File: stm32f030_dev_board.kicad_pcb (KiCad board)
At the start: 4 copper layers, 85 x 55 mm, 66 parts, among them J2 Conn_01x16, J3 Conn_01x16, J4 Conn_01x16, J5 Conn_01x06, J6 Conn_01x04, J7 USB_C_Receptacle_USB2.0_16P, Q1 DMP3099L, Q2 DMP3099L, SW1 SW_Push, SW3 SW_Push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

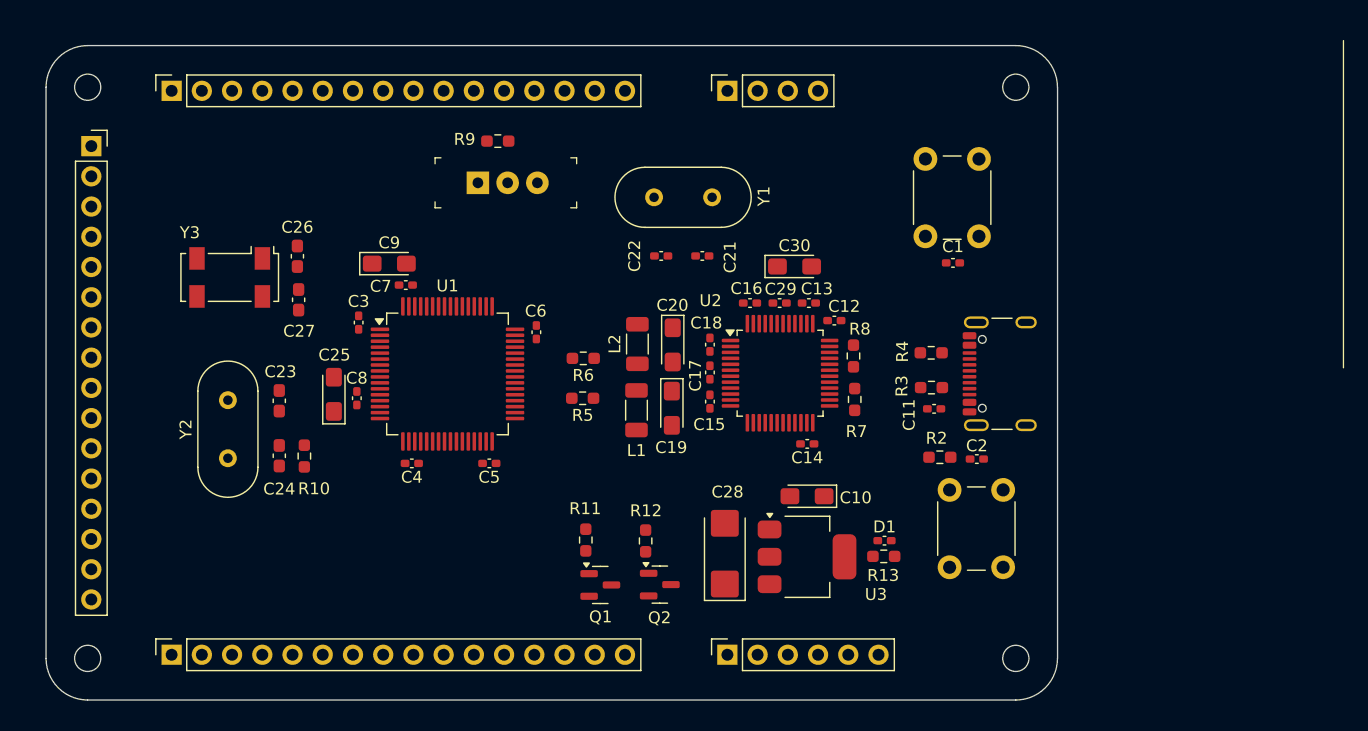
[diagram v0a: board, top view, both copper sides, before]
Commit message: Adjusted Spacing between pin headers
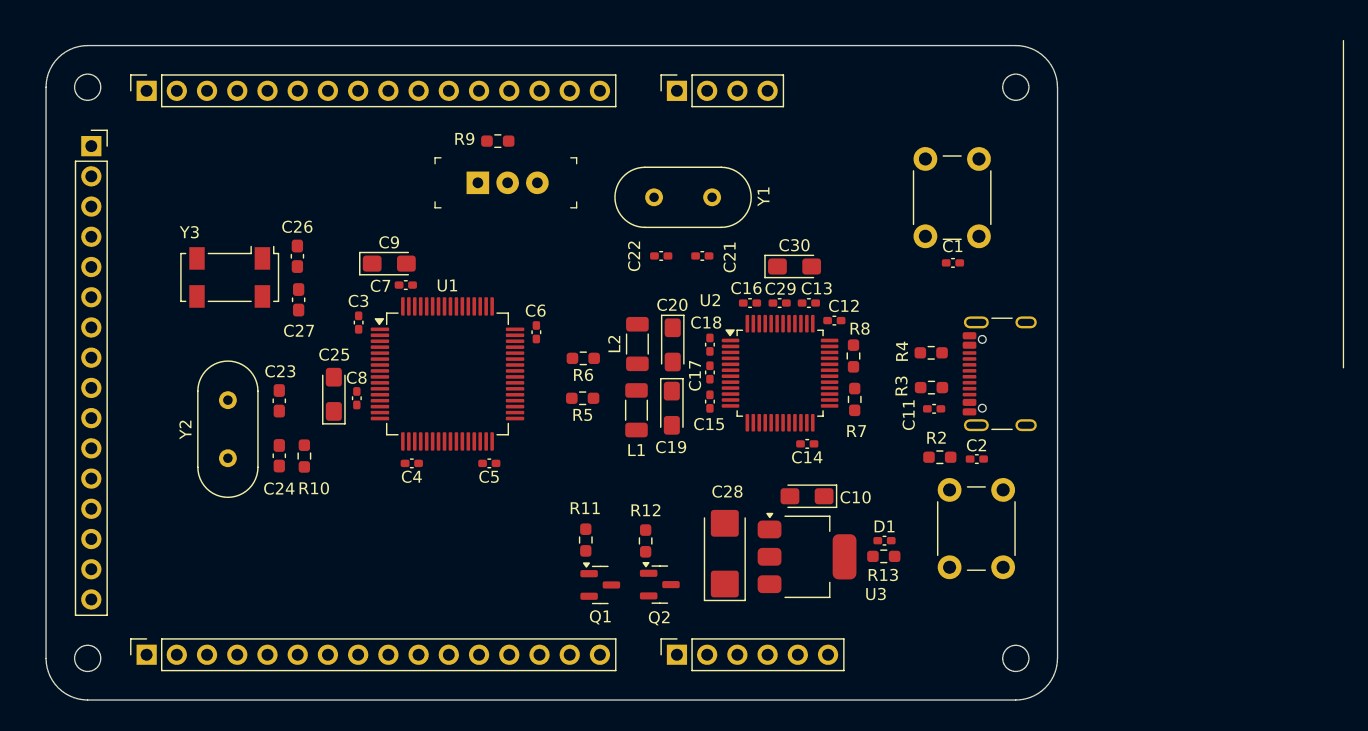
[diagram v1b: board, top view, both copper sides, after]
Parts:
- moved J5 4.24 mm to (143.0, 121.2)
- moved J6 4.24 mm to (143.0, 73.8)
- moved J2 2.11 mm to (98.5, 121.2)
- moved J3 2.11 mm to (98.5, 73.8)
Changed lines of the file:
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@@
 	(footprint "Connector_PinSocket_2.54mm:PinSocket_1x04_P2.54mm_Vertical"
 		(layer "F.Cu")
-		(at 147.26 73.803 90)
+		(at 143.02 73.803 90)
 		(descr "Through hole straight socket strip, 1x04, 2.54mm pitch, single row (from Kicad 4.0.7), script generated")
 		(tags "Through hole socket strip THT 1x04 2.54mm single row")
@@
 			(at 0 10.39 90)
 			(layer "F.Fab")
+			(hide yes)
 			(effects
 				(font
@@
 	(footprint "Connector_PinSocket_2.54mm:PinSocket_1x06_P2.54mm_Vertical"
 		(layer "F.Cu")
-		(at 147.26 121.197 90)
+		(at 143.02 121.197 90)
 		(descr "Through hole straight socket strip, 1x06, 2.54mm pitch, single row (from Kicad 4.0.7), script generated")
 		(tags "Through hole socket strip THT 1x06 2.54mm single row")
@@
 			(at 0 3.2 0)
 			(layer "F.Fab")
+			(hide yes)
 			(effects
 				(font
@@
 			(unlocked yes)
 			(layer "F.Fab")
+			(hide yes)
 			(effects
 				(font
@@
 	(footprint "Connector_PinSocket_2.54mm:PinSocket_1x16_P2.54mm_Vertical"
 		(layer "F.Cu")
-		(at 100.555 73.803 90)
+		(at 98.45 73.803 90)
 		(descr "Through hole straight socket strip, 1x16, 2.54mm pitch, single row (from Kicad 4.0.7), script generated")
 		(tags "Through hole socket strip THT 1x16 2.54mm single row")
@@
 			(at 0 40.87 90)
 			(layer "F.Fab")
+			(hide yes)
 			(effects
 				(font
@@
 	(footprint "Connector_PinSocket_2.54mm:PinSocket_1x16_P2.54mm_Vertical"
 		(layer "F.Cu")
-		(at 100.555 121.197 90)
+		(at 98.45 121.197 90)
 		(descr "Through hole straight socket strip, 1x16, 2.54mm pitch, single row (from Kicad 4.0.7), script generated")
 		(tags "Through hole socket strip THT 1x16 2.54mm single row")
@@
 			(at 0 3.2 0)
 			(layer "F.Fab")
+			(hide yes)
 			(effects
 				(font

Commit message: removed D+ and D- resistors, finished routing front and back copper, moved button to better place
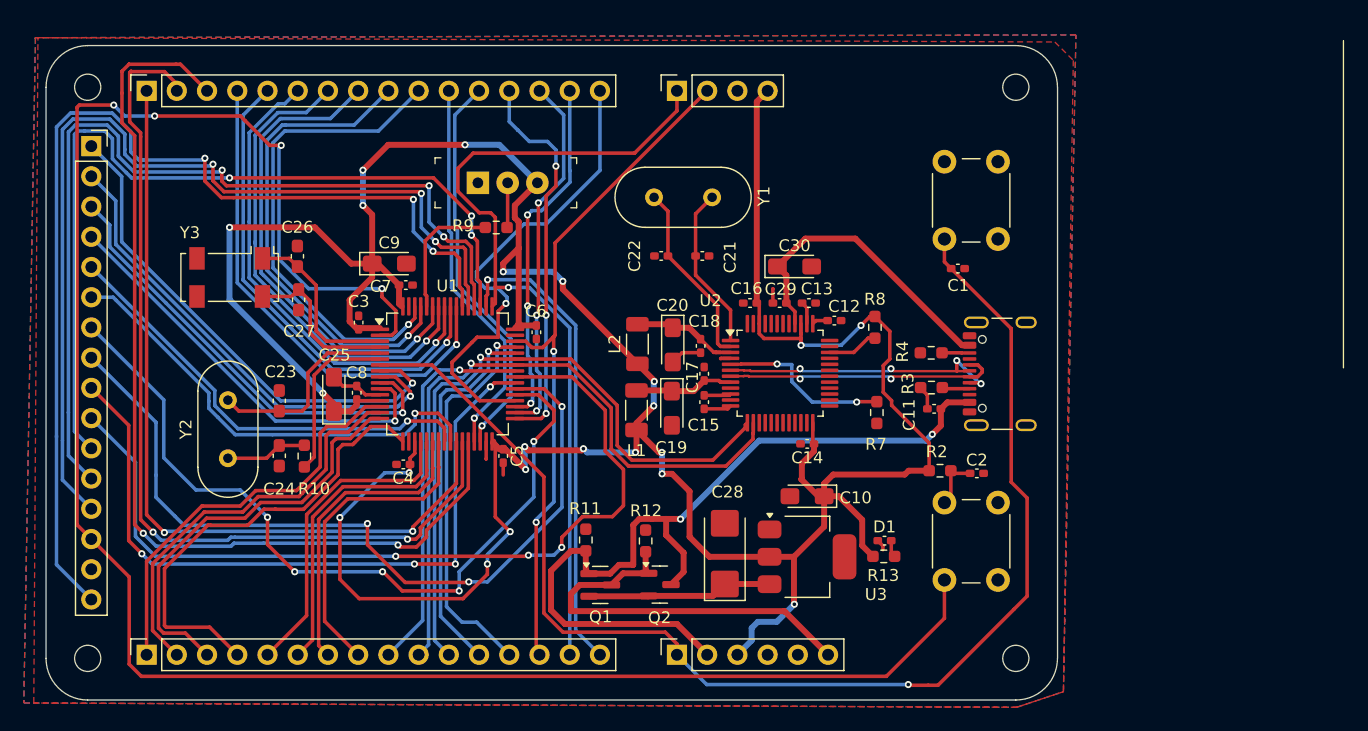
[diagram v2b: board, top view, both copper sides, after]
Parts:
- removed R5, R6: 22, Resistor_SMD:R_0603_1608Metric_Pad0.98x0.95mm_HandSolder
- moved R9 7.26 mm to (127.8, 85.3)
- moved R8 3.01 mm to (159.7, 93.7)
- moved R7 2.16 mm to (159.8, 100.8), turned to -90 degrees
- moved SW1 1.61 mm to (170.0, 79.8)
- moved C5 1.32 mm to (128.4, 104.5), turned to -90 degrees
- moved C2 1.20 mm to (168.2, 106.0)
- moved SW3 1.15 mm to (170.0, 108.4)
- moved R2 1.13 mm to (165.1, 105.7)
- moved C18 0.79 mm to (145.0, 95.2)
- moved C4 0.72 mm to (120.0, 105.2)
- moved C1 0.63 mm to (166.6, 88.7)
- moved C17 0.50 mm to (145.3, 97.6)
- moved C15 0.48 mm to (145.3, 100.0)
- moved C8 0.46 mm to (116.1, 99.2)
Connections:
- J4 pad 15: unconnected-(J4-Pin_15-Pad15) -> GND
- U2 pad 6: /DM -> /D-
- U2 pad 7: /DP -> /D+
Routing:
- net +3.3V: track 0.00 -> 288.2 mm, vias 0 -> 22
- net /PC13: track 0.00 -> 170.9 mm, vias 0 -> 4
- net /NRST: track 0.00 -> 108.8 mm, vias 0 -> 1
- net +5V: track 0.00 -> 97.2 mm, vias 0 -> 2
- net /PD2: track 0.00 -> 88.3 mm, vias 0 -> 3
- net /PB2: track 0.00 -> 82.2 mm, vias 0 -> 2
- net /PC12: track 0.00 -> 80.1 mm, vias 0 -> 3
- net /PC11: track 0.00 -> 76.9 mm, vias 0 -> 3
- net /PB1: track 0.00 -> 76.9 mm, vias 0 -> 2
- net /PC9: track 0.00 -> 72.8 mm, vias 0 -> 3
- net /PC10: track 0.00 -> 72.3 mm, vias 0 -> 3
- net /SWCLK: track 0.00 -> 70.8 mm, vias 0 -> 1
- net /PC7: track 0.00 -> 67.9 mm, vias 0 -> 3
- net /PB0: track 0.00 -> 67.7 mm, vias 0 -> 2
- net /PC6: track 0.00 -> 66.6 mm, vias 0 -> 5
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- added copper zone on B.Cu, net GND
- added copper zone on F.Cu, net GND
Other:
- copper layers 4 -> 2

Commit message: Finished routing, Added silk screen labels for ports, fixed USB C footprint(removed stacked pads for ground pins)
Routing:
- net GND: track 16.9 -> 107.8 mm, vias 0 -> 20
- net +5V: track 97.2 -> 105.9 mm, vias 2 -> 4
- net +3.3V: track 288.2 -> 296.8 mm
- net /PC13: track 170.9 -> 177.4 mm
- net /NRST: track 108.8 -> 115.3 mm
- net /PB15: track 40.0 -> 39.0 mm
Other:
- board text added: "3.3V"
- board text added: "5V"
- board text added: "GND"
- board text added: "NRST"
- board text added: "PA0"
- board text added: "PA1"
- board text added: "PA10(USART1_RX)"
- board text added: "PA11"
- board text added: "PA12"
- board text added: "PA13(SWDIO)"
- board text added: "PA15"
- board text added: "PA15(SWCLK)"
- board text added: "PA2"
- board text added: "PA3"
- board text added: "PA4"
- board text added: "PA5"
- board text added: "PA6"
- board text added: "PA7"
- board text added: "PA8"
- board text added: "PA9(USART1_TX)"
- board text added: "PB0"
- board text added: "PB1"
- board text added: "PB10"
- board text added: "PB11"
- board text added: "PB12"
- board text added: "PB13"
- board text added: "PB14"
- board text added: "PB15"
- board text added: "PB2"
- board text added: "PB3"
- board text added: "PB4"
- board text added: "PB5"
- board text added: "PB6"
- board text added: "PB7"
- board text added: "PB8"
- board text added: "PB9"
- board text added: "PC0"
- board text added: "PC1"
- board text added: "PC10"
- board text added: "PC11"
- board text added: "PC12"
- board text added: "PC13"
- board text added: "PC2"
- board text added: "PC3"
- board text added: "PC4"
- board text added: "PC5"
- board text added: "PC6"
- board text added: "PC7"
- board text added: "PC8"
- board text added: "PC9"
- board text added: "PD2"
- board text added: "RESET"
- board text added: "SWCLK"
- board text added: "SWDIO"
- board text added: "User Button"
- board text added: "VIN"

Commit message: fixed silkscreen overlap and updated .gitignore
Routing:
- net GND: vias 20 -> 19
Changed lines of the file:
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@@
 			(plot_on_all_layers_selection 0x00000000_00000000_00000000_00000000)
 			(disableapertmacros no)
-			(usegerberextensions no)
-			(usegerberattributes yes)
-			(usegerberadvancedattributes yes)
-			(creategerberjobfile yes)
+			(usegerberextensions yes)
+			(usegerberattributes no)
+			(usegerberadvancedattributes no)
+			(creategerberjobfile no)
 			(dashed_line_dash_ratio 12.000000)
 			(dashed_line_gap_ratio 3.000000)
@@
 			(sketchdnponfab yes)
 			(crossoutdnponfab yes)
-			(subtractmaskfromsilk no)
+			(subtractmaskfromsilk yes)
 			(outputformat 1)
 			(mirror no)
-			(drillshape 1)
+			(drillshape 0)
 			(scaleselection 1)
-			(outputdirectory "")
+			(outputdirectory "gerber_files/")
 		)
 	)
@@
 	)
 	(gr_text "PA1\n"
-		(at 100.43 117.08 270)
+		(at 100.47 116.97 270)
 		(layer "F.SilkS")
 		(effects
@@
 	)
 	(gr_text "3.3V"
-		(at 147.23 116.56 270)
+		(at 147.43 116.69 270)
 		(layer "F.SilkS")
 		(effects
 			(font
-				(size 1 1)
+				(size 1 0.95)
 				(thickness 0.1)
 			)
@@
 	)
 	(gr_text "PA10(USART1_RX)\n"
-		(at 123.34 106.55 270)
+		(at 123.38 106.5 270)
 		(layer "F.SilkS")
 		(effects
@@
 		(net 2)
 	)
-	(via
-		(at 158.3 79.87)
-		(size 0.6)
-		(drill 0.3)
-		(layers "F.Cu" "B.Cu")
-		(free yes)
-		(net 2)
-	)

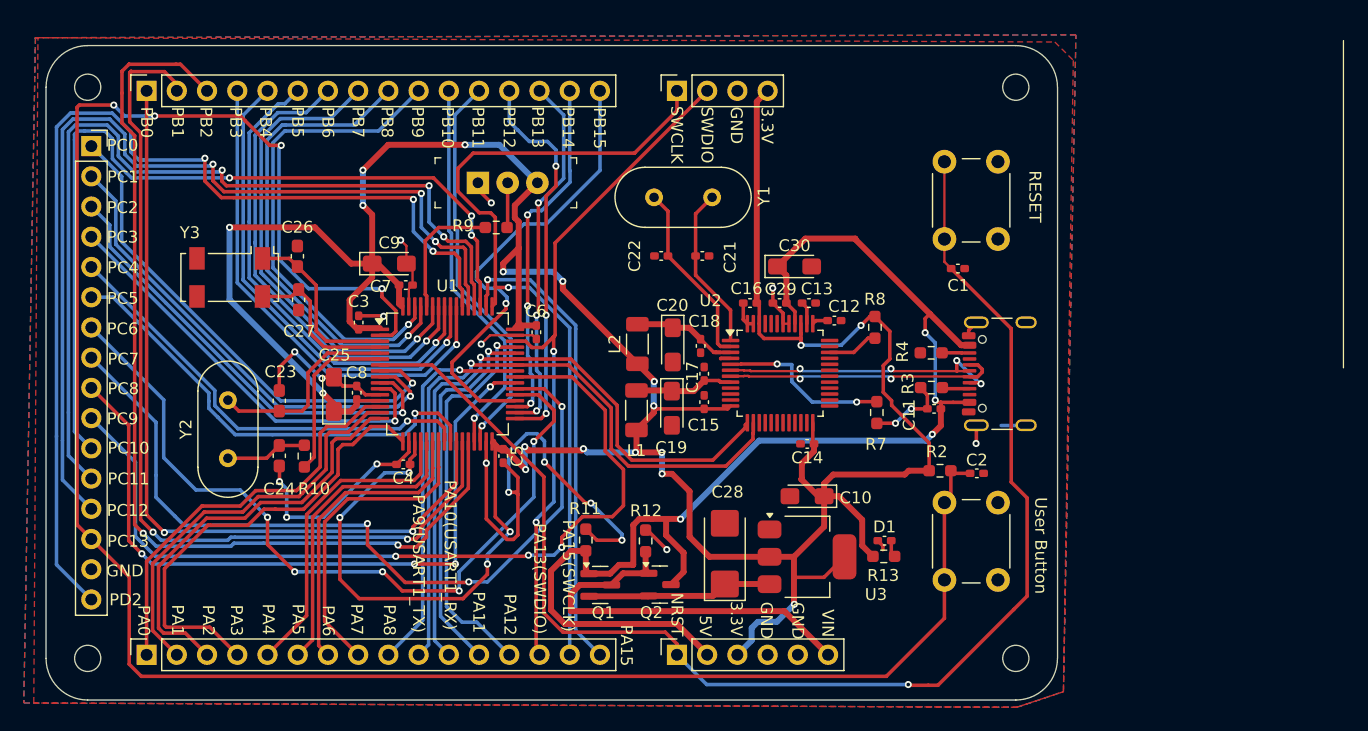
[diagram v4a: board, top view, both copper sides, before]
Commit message: Switched to 4 layer board stackup and rerouted
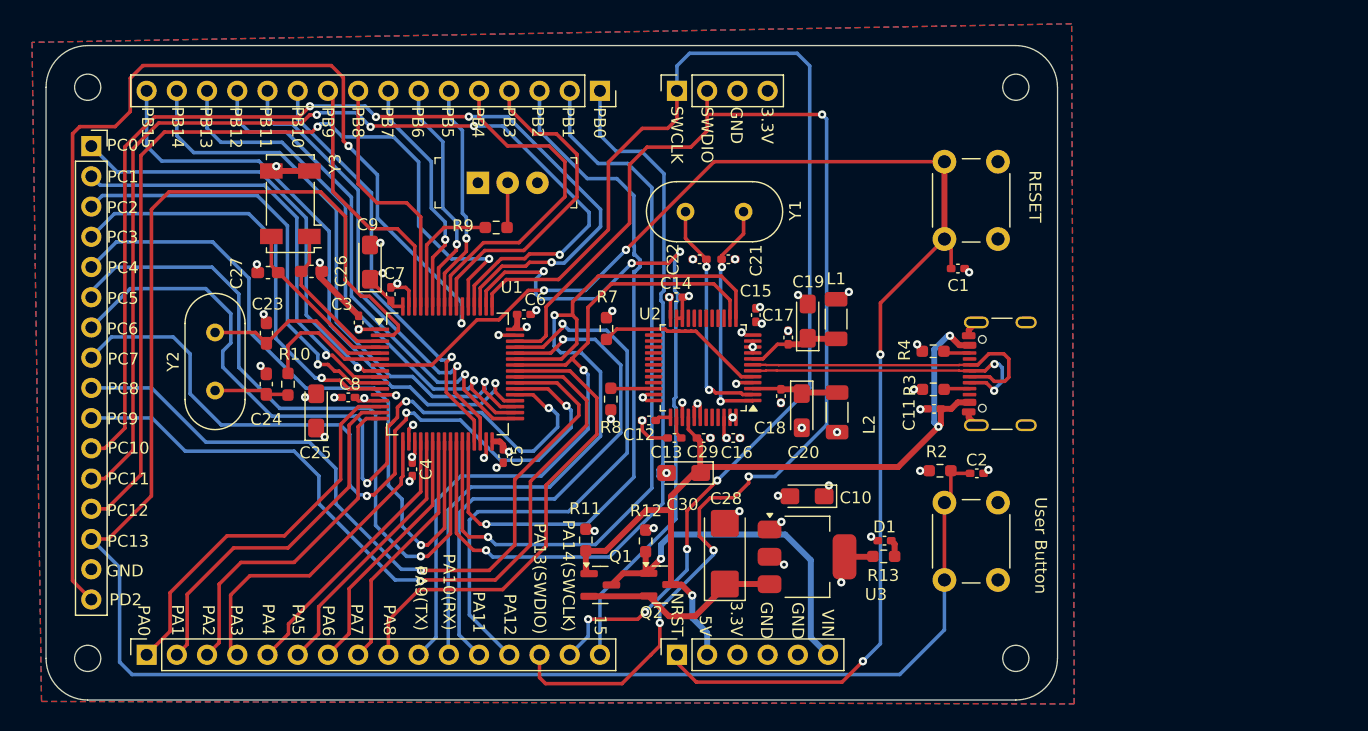
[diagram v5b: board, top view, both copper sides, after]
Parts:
- moved J3 38.1 mm to (136.6, 73.8), turned to -90 degrees
- moved R7 23.8 mm to (137.1, 93.8), turned to 90 degrees
- moved R8 23.0 mm to (137.5, 99.7), turned to -90 degrees
- moved C30 19.7 mm to (143.6, 105.9), turned to 180 degrees
- moved L1 18.4 mm to (156.4, 93.0), turned to -90 degrees
- moved L2 17.7 mm to (156.5, 100.8)
- moved C12 17.7 mm to (140.7, 101.5), turned to 0 degrees
- moved C14 16.5 mm to (142.9, 91.1), turned to 0 degrees
- moved C13 16.0 mm to (142.8, 103.0), turned to 0 degrees
- moved C19 13.6 mm to (154.0, 93.2), turned to 90 degrees
- moved C29 13.0 mm to (145.3, 103.0), turned to 0 degrees
- moved C20 12.2 mm to (153.5, 100.7)
- moved C16 11.4 mm to (147.8, 103.0), turned to 0 degrees
- moved C15 8.51 mm to (149.6, 92.6)
- moved Y3 8.02 mm to (110.5, 83.3), turned to 180 degrees
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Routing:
- net +3.3V: track 296.8 -> 20.4 mm, vias 22 -> 19
- net GND: track 107.8 -> 30.8 mm, vias 19 -> 45
- net /SWDIO: track 57.3 -> 108.4 mm, vias 2 -> 4
- net +5V: track 105.9 -> 69.9 mm, vias 4 -> 3
- net /SWCLK: track 70.8 -> 102.8 mm, vias 1 -> 4
- net /PB2: track 82.2 -> 59.7 mm, vias 2 -> 1
- net /PB5: track 40.6 -> 19.5 mm
- net /PB6: track 40.7 -> 20.1 mm
- net /PC5: track 38.8 -> 59.2 mm
- net /PB7: track 40.7 -> 20.5 mm
- net /PA15: track 39.8 -> 59.9 mm, vias 1 -> 3
- net /PC4: track 37.7 -> 57.0 mm
- net /PB14: track 29.9 -> 49.1 mm, vias 3 -> 1
- net /PB8: track 40.6 -> 21.8 mm, vias 1 -> 0
- net /PB9: track 40.7 -> 22.5 mm, vias 1 -> 0
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- added copper zone on In2.Cu, net +3.3V
- added copper zone on In1.Cu, net GND
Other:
- copper layers 2 -> 4
- board text added: "15"
- board text added: "PA10(RX)"
- board text added: "PA14(SWCLK)"
- board text added: "PA9(TX)"
- board text removed: "PA10(USART1_RX)"
- board text removed: "PA15"
- board text removed: "PA15(SWCLK)"
- board text removed: "PA9(USART1_TX)"
